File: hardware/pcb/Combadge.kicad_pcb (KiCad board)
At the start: 2 copper layers, 45 x 31 mm, 27 parts, among them J1 Conn_01x05_Female, J2 USB_B_Micro, J3 TOUCH, U1 XC6808A4D28R-G, U2 ESP32-WROOM-32, U3 NCP160AMX330TBG, U4 NAU8315YG

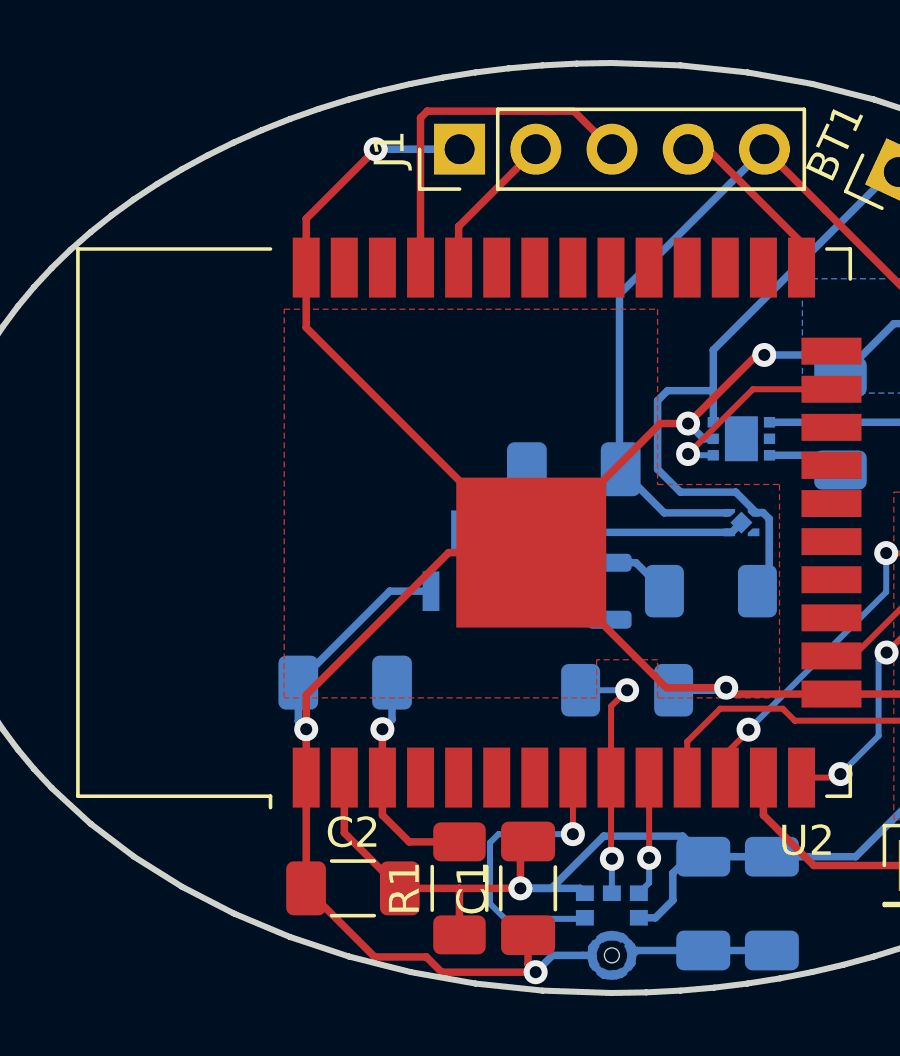
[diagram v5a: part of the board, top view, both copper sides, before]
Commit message: Change ground plane to reduce stray capacitances
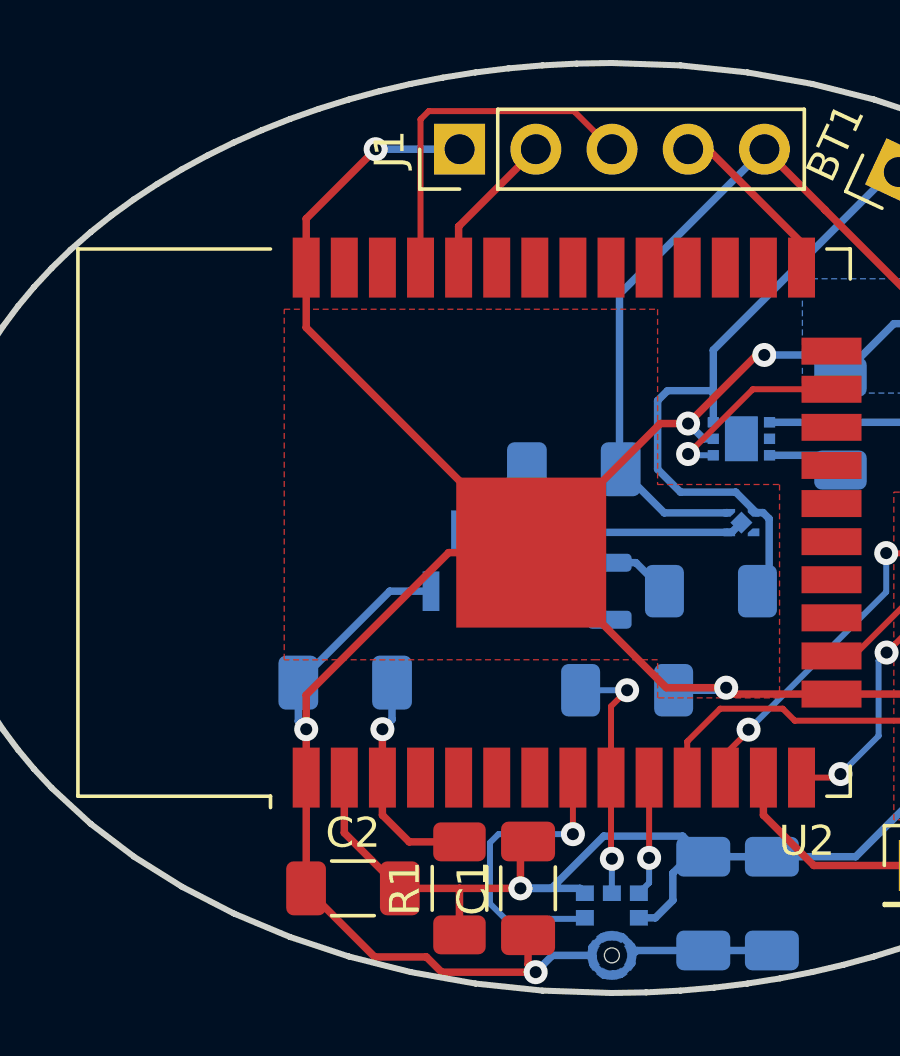
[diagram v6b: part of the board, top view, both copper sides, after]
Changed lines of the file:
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@@
   (net 52 "unconnected-(U4-Pad10)")
   (net 53 "unconnected-(U4-Pad15)")
-  (net 54 "Net-(R4-Pad2)")
+  (net 54 "Net-(D1-Pad1)")
   (net 55 "unconnected-(D1-Pad2)")
-  (net 56 "Net-(MOSFET1-Pad1)")
+  (net 56 "Net-(D1-Pad3)")
   (footprint "Connector_PinHeader_2.54mm:PinHeader_1x02_P2.54mm_Vertical" (layer "F.Cu")
     (at 84.747818 49.276 65)
@@
       (net 1 "+BATT") (pintype "passive"))
     (pad "2" smd roundrect (at 1.55 0 180) (size 1.3 1.75) (layers "B.Cu" "B.Paste" "B.Mask") (roundrect_rratio 0.192308)
-      (net 54 "Net-(R4-Pad2)") (pintype "passive"))
+      (net 54 "Net-(D1-Pad1)") (pintype "passive"))
     (model "${KICAD6_3DMODEL_DIR}/Resistor_SMD.3dshapes/R_1206_3216Metric.wrl"
       (offset (xyz 0 0 0))
@@
     (fp_line (start -0.65 -1.45) (end -0.65 1.125) (layer "B.Fab") (width 0.1))
     (pad "1" smd roundrect (at -0.9375 0.95 180) (size 1.475 0.6) (layers "B.Cu" "B.Paste" "B.Mask") (roundrect_rratio 0.25)
-      (net 54 "Net-(R4-Pad2)") (pinfunction "K") (pintype "passive"))
+      (net 54 "Net-(D1-Pad1)") (pinfunction "K") (pintype "passive"))
     (pad "2" smd roundrect (at -0.9375 -0.95 180) (size 1.475 0.6) (layers "B.Cu" "B.Paste" "B.Mask") (roundrect_rratio 0.25)
       (net 55 "unconnected-(D1-Pad2)") (pinfunction "K") (pintype "passive"))
     (pad "3" smd roundrect (at 0.9375 0 180) (size 1.475 0.6) (layers "B.Cu" "B.Paste" "B.Mask") (roundrect_rratio 0.25)
-      (net 56 "Net-(MOSFET1-Pad1)") (pinfunction "A") (pintype "passive"))
+      (net 56 "Net-(D1-Pad3)") (pinfunction "A") (pintype "passive"))
     (model "${KICAD6_3DMODEL_DIR}/Package_TO_SOT_SMD.3dshapes/SOT-23.wrl"
       (offset (xyz 0 0 0))
@@
     (fp_circle (center -1.27 -0.4445) (end -1.143 -0.4445) (layer "B.Fab") (width 0.1) (fill none))
     (pad "1" smd rect locked (at -0.950001 -1.016 180) (size 0.5588 1.3208) (layers "B.Cu" "B.Paste" "B.Mask")
-      (net 56 "Net-(MOSFET1-Pad1)") (pinfunction "1") (pintype "unspecified"))
+      (net 56 "Net-(D1-Pad3)") (pinfunction "1") (pintype "unspecified"))
     (pad "2" smd rect locked (at 0.950001 -1.016 180) (size 0.5588 1.3208) (layers "B.Cu" "B.Paste" "B.Mask")
       (net 2 "GND") (pinfunction "2") (pintype "unspecified"))
@@
   (segment (start 75.184 74.7235) (end 75.221499 74.760999) (width 0.25) (layer "B.Cu") (net 2))
   (segment (start 76.01 75.2225) (end 75.8465 75.386) (width 0.25) (layer "B.Cu") (net 2))
-  (segment (start 74.22 75.386) (end 74.5215 75.386) (width 0.25) (layer "B.Cu") (net 2))
+  (segment (start 73.204 75.386) (end 74.5215 75.386) (width 0.25) (layer "B.Cu") (net 2))
   (segment (start 75.221499 74.760999) (end 75.522999 74.760999) (width 0.25) (layer "B.Cu") (net 2))
   (segment (start 75.4888 76.011001) (end 75.8465 75.653301) (width 0.25) (layer "B.Cu") (net 2))
@@
   (segment (start 74.558999 75.692) (end 74.915499 76.0485) (width 0.25) (layer "B.Cu") (net 2))
   (segment (start 78.908666 66.548) (end 77.242 66.548) (width 0.25) (layer "B.Cu") (net 2))
-  (segment (start 73.204 75.386) (end 74.22 75.386) (width 0.25) (layer "B.Cu") (net 2))
   (segment (start 75.221499 76.011001) (end 75.4888 76.011001) (width 0.25) (layer "B.Cu") (net 2))
   (segment (start 75.184 76.0485) (end 75.221499 76.011001) (width 0.25) (layer "B.Cu") (net 2))
@@
   (segment (start 70.075 51.088) (end 70.075 52.46) (width 0.25) (layer "F.Cu") (net 6))
   (segment (start 72.649 48.514) (end 70.075 51.088) (width 0.25) (layer "F.Cu") (net 6))
-  (segment (start 68.805 52.46) (end 68.805 47.468) (width 0.25) (layer "F.Cu") (net 7))
-  (segment (start 68.805 47.468) (end 69.029 47.244) (width 0.25) (layer "F.Cu") (net 7))
-  (segment (start 69.029 47.244) (end 73.919 47.244) (width 0.25) (layer "F.Cu") (net 7))
-  (segment (start 73.919 47.244) (end 75.189 48.514) (width 0.25) (layer "F.Cu") (net 7))
+  (segment (start 68.805 47.518) (end 69.079 47.244) (width 0.2) (layer "F.Cu") (net 7))
+  (segment (start 69.079 47.244) (end 73.919 47.244) (width 0.2) (layer "F.Cu") (net 7))
+  (segment (start 73.919 47.244) (end 75.189 48.514) (width 0.2) (layer "F.Cu") (net 7))
+  (segment (start 68.805 52.46) (end 68.805 47.518) (width 0.2) (layer "F.Cu") (net 7))
   (segment (start 78.389 48.514) (end 81.505 51.63) (width 0.25) (layer "F.Cu") (net 8))
   (segment (start 92.202 59.944) (end 93.715 59.944) (width 0.25) (layer "B.Cu") (net 9))
@@
         (xy 76.708 65.532)
         (xy 74.676 65.532)
-        (xy 74.676 66.802)
-        (xy 64.262 66.802)
+        (xy 74.676 65.532)
+        (xy 64.262 65.532)
         (xy 64.262 53.848)
         (xy 76.708 53.848)

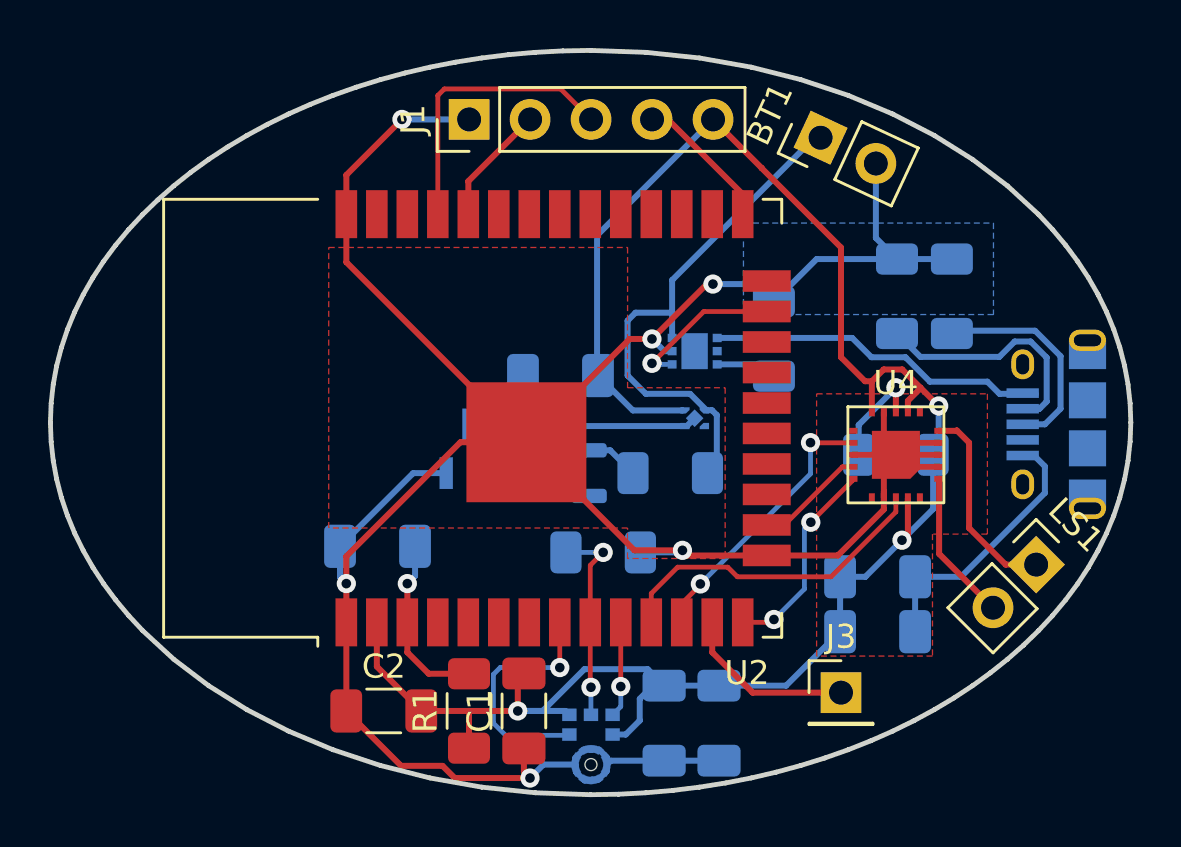
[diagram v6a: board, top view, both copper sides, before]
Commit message: Add PCB cutout SVG
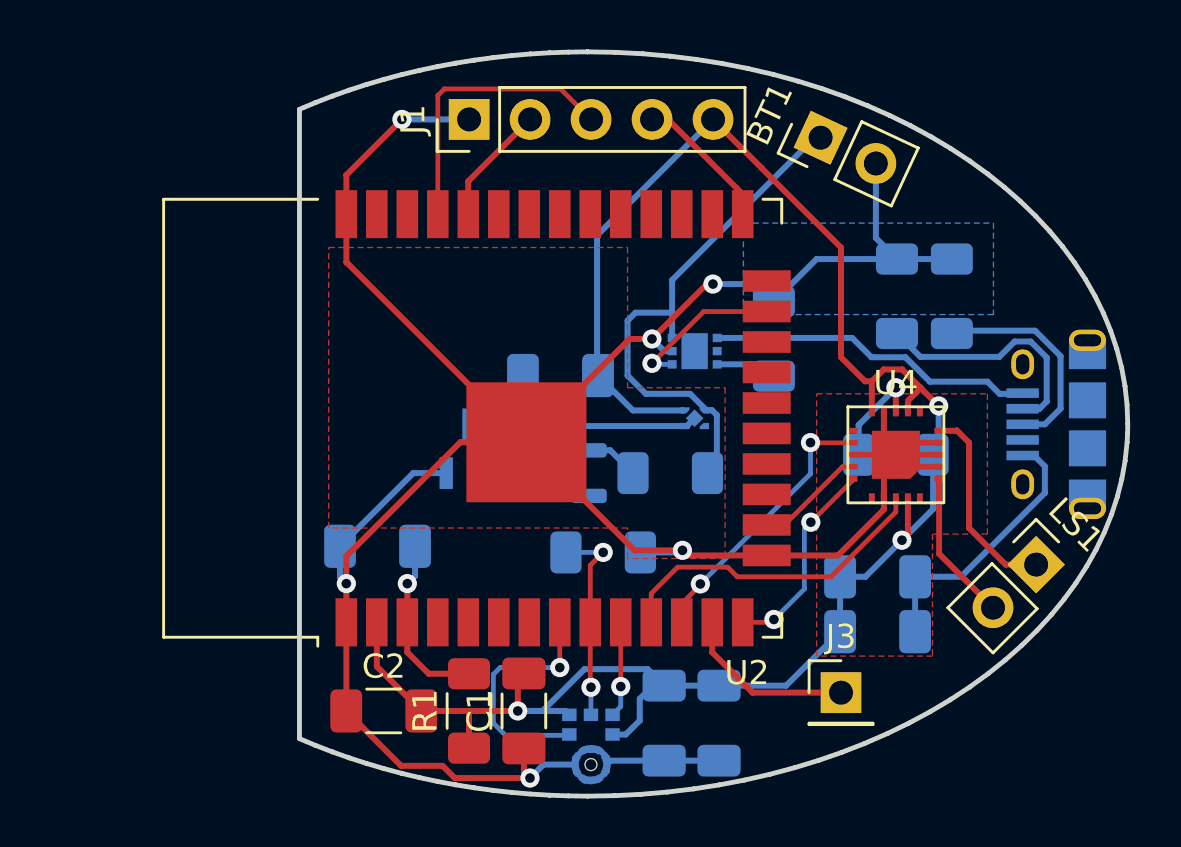
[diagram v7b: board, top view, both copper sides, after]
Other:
- board size 45 x 31 mm -> 34.5 x 31 mm
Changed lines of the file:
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@@
   (gr_poly
     (pts
-      (xy 77.47 45.72)
-      (xy 79.70404 45.95488)
-      (xy 81.860316 46.336824)
-      (xy 83.927519 46.858042)
-      (xy 85.89434 47.510741)
-      (xy 87.749467 48.287131)
-      (xy 89.481592 49.179421)
-      (xy 91.079405 50.17982)
-      (xy 92.531597 51.280535)
-      (xy 93.826856 52.473777)
-      (xy 94.412102 53.102661)
-      (xy 94.953874 53.751754)
-      (xy 95.450758 54.420084)
-      (xy 95.901341 55.106675)
-      (xy 96.304208 55.810555)
-      (xy 96.657947 56.530749)
-      (xy 96.961143 57.266283)
-      (xy 97.212382 58.016184)
-      (xy 97.410252 58.779478)
-      (xy 97.553337 59.55519)
-      (xy 97.640226 60.342347)
-      (xy 97.669502 61.139975)
-      (xy 97.640226 61.937603)
-      (xy 97.553337 62.72476)
-      (xy 97.410252 63.500472)
-      (xy 97.212382 64.263766)
-      (xy 96.961143 65.013666)
-      (xy 96.657947 65.749201)
-      (xy 96.304208 66.469395)
-      (xy 95.901341 67.173274)
-      (xy 95.450758 67.859866)
-      (xy 94.953874 68.528195)
-      (xy 94.412102 69.177289)
-      (xy 93.826856 69.806172)
-      (xy 93.19955 70.413872)
-      (xy 92.531597 70.999414)
-      (xy 91.824411 71.561825)
-      (xy 91.079405 72.10013)
-      (xy 90.297995 72.613356)
-      (xy 89.481592 73.100528)
-      (xy 88.631612 73.560674)
-      (xy 87.749467 73.992818)
-      (xy 86.836572 74.395988)
-      (xy 85.89434 74.769209)
-      (xy 84.924184 75.111507)
-      (xy 83.927519 75.421908)
-      (xy 82.905759 75.699439)
-      (xy 81.860316 75.943126)
-      (xy 80.792605 76.151994)
-      (xy 79.70404 76.32507)
-      (xy 78.596033 76.46138)
-      (xy 77.47 76.55995)
-      (xy 76.327353 76.619807)
-      (xy 75.169506 76.639975)
-      (xy 72.869012 76.55995)
-      (xy 70.634972 76.32507)
-      (xy 68.478696 75.943126)
-      (xy 66.411492 75.421908)
-      (xy 64.444672 74.769209)
-      (xy 62.589544 73.992818)
-      (xy 60.857419 73.100528)
-      (xy 59.259606 72.10013)
-      (xy 57.807415 70.999414)
-      (xy 56.512156 69.806172)
-      (xy 55.92691 69.177289)
-      (xy 55.385138 68.528195)
-      (xy 54.888254 67.859866)
-      (xy 54.437671 67.173274)
-      (xy 54.034804 66.469395)
-      (xy 53.681065 65.749201)
-      (xy 53.377869 65.013666)
-      (xy 53.12663 64.263766)
-      (xy 52.928761 63.500472)
-      (xy 52.785675 62.72476)
-      (xy 52.698787 61.937603)
-      (xy 52.66951 61.139975)
-      (xy 52.698787 60.342347)
-      (xy 52.785675 59.55519)
-      (xy 52.928761 58.779478)
-      (xy 53.12663 58.016184)
-      (xy 53.377869 57.266283)
-      (xy 53.681065 56.530749)
-      (xy 54.034804 55.810555)
-      (xy 54.437671 55.106675)
-      (xy 54.888254 54.420084)
-      (xy 55.385138 53.751754)
-      (xy 55.92691 53.102661)
-      (xy 56.512156 52.473777)
-      (xy 57.139462 51.866078)
-      (xy 57.807415 51.280535)
-      (xy 58.514601 50.718125)
-      (xy 59.259606 50.17982)
-      (xy 60.041017 49.666594)
-      (xy 60.857419 49.179421)
-      (xy 61.7074 48.719276)
-      (xy 62.589544 48.287131)
-      (xy 63.50244 47.883962)
-      (xy 64.444672 47.510741)
-      (xy 65.414827 47.168443)
-      (xy 66.411492 46.858042)
-      (xy 67.433253 46.580511)
-      (xy 68.478696 46.336824)
-      (xy 69.546406 46.127956)
-      (xy 70.634972 45.95488)
-      (xy 71.742979 45.81857)
-      (xy 72.869012 45.72)
-      (xy 74.011659 45.660144)
-      (xy 75.169506 45.639975)
+      (xy 76.2 45.72)
+      (xy 77.342635 45.779866)
+      (xy 78.468656 45.878445)
+      (xy 79.576649 46.014764)
+      (xy 80.665202 46.187847)
+      (xy 81.732899 46.396722)
+      (xy 82.778328 46.640414)
+      (xy 83.800075 46.917949)
+      (xy 84.796727 47.228353)
+      (xy 85.766868 47.570654)
+      (xy 86.709087 47.943876)
+      (xy 87.621969 48.347045)
+      (xy 88.5041 48.779189)
+      (xy 89.354068 49.239332)
+      (xy 90.170457 49.726501)
+      (xy 90.951855 50.239723)
+      (xy 91.696848 50.778023)
+      (xy 92.404022 51.340427)
+      (xy 93.071964 51.925961)
+      (xy 93.69926 52.533652)
+      (xy 94.284495 53.162526)
+      (xy 94.826258 53.811608)
+      (xy 95.323133 54.479925)
+      (xy 95.773708 55.166503)
+      (xy 96.176568 55.870368)
+      (xy 96.530299 56.590546)
+      (xy 96.83349 57.326063)
+      (xy 97.084724 58.075946)
+      (xy 97.28259 58.83922)
+      (xy 97.425673 59.614911)
+      (xy 97.512559 60.402046)
+      (xy 97.541835 61.19965)
+      (xy 97.534919 61.584528)
+      (xy 97.514207 61.968261)
+      (xy 97.431783 62.731655)
+      (xy 97.295325 63.488563)
+      (xy 97.105598 64.237714)
+      (xy 96.863366 64.977838)
+      (xy 96.569393 65.707663)
+      (xy 96.224442 66.42592)
+      (xy 95.829278 67.131337)
+      (xy 95.384664 67.822645)
+      (xy 94.891365 68.498573)
+      (xy 94.350143 69.157851)
+      (xy 93.761764 69.799207)
+      (xy 93.12699 70.421371)
+      (xy 92.446586 71.023074)
+      (xy 91.721316 71.603043)
+      (xy 90.951944 72.16001)
+      (xy 90.143464 72.690036)
+      (xy 89.301591 73.189681)
+      (xy 88.42817 73.658419)
+      (xy 87.525045 74.095723)
+      (xy 86.594059 74.501068)
+      (xy 85.637058 74.873926)
+      (xy 84.655885 75.213772)
+      (xy 83.652386 75.52008)
+      (xy 82.628403 75.792322)
+      (xy 81.585781 76.029973)
+      (xy 80.526365 76.232507)
+      (xy 79.451999 76.399397)
+      (xy 78.364527 76.530117)
+      (xy 77.265793 76.624141)
+      (xy 76.157642 76.680943)
+      (xy 75.041918 76.699995)
+      (xy 74.246612 76.690016)
+      (xy 73.454059 76.660764)
+      (xy 72.664965 76.61238)
+      (xy 71.880033 76.545005)
+      (xy 71.09997 76.458779)
+      (xy 70.32548 76.353842)
+      (xy 69.557267 76.230336)
+      (xy 68.796037 76.088401)
+      (xy 68.042493 75.928177)
+      (xy 67.297342 75.749806)
+      (xy 66.561288 75.553427)
+      (xy 65.835034 75.339181)
+      (xy 65.119288 75.10721)
+      (xy 64.414752 74.857652)
+      (xy 63.722132 74.59065)
+      (xy 63.042133 74.306344)
+      (xy 63.04213 48.092955)
+      (xy 63.722143 47.808682)
+      (xy 64.414775 47.541714)
+      (xy 65.11932 47.29219)
+      (xy 65.835075 47.060252)
+      (xy 66.561334 46.84604)
+      (xy 67.297393 46.649694)
+      (xy 68.042547 46.471356)
+      (xy 68.796091 46.311165)
+      (xy 69.557321 46.169262)
+      (xy 70.325531 46.045788)
+      (xy 71.100017 45.940884)
+      (xy 71.880074 45.854689)
+      (xy 72.664997 45.787345)
+      (xy 73.454082 45.738991)
+      (xy 74.246624 45.70977)
+      (xy 75.041918 45.69982)
+      (xy 75.042165 45.69982)
     ) (layer "Edge.Cuts") (width 0.2) (fill none))
   (segment (start 79.313316 59.944) (end 79.995658 60.626342) (width 0.25) (layer "B.Cu") (net 1))
@@
         (xy 76.708 65.532)
         (xy 74.676 65.532)
-        (xy 74.676 65.532)
         (xy 64.262 65.532)
         (xy 64.262 53.848)
@@
     )
   )
-  (group "" (id 587dcd05-814f-42d9-95ca-65a9807404c3)
+  (group "" (id 4c75cbca-1ba8-443a-be26-16942643866c)
     (members
-      765f55d7-54da-4b53-98de-a3e8d9987e35
+      a39aee15-43e9-4040-8939-37de0f83e0b7
     )
   )
